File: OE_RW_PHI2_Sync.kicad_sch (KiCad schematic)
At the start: 2 parts, among them U5 74LS08, U9 74HC04

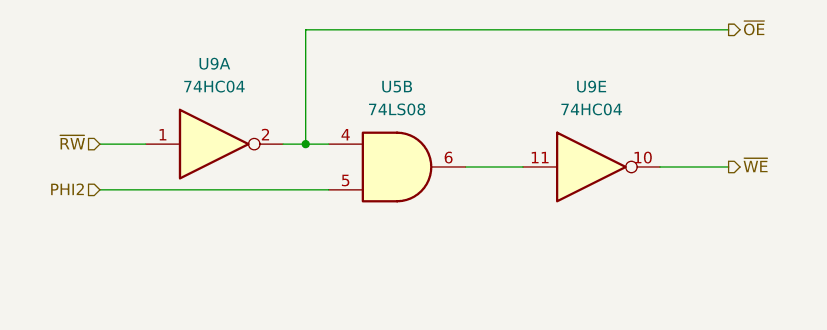
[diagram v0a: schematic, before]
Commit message: Rev 1 power section: run everything from the Pico's USB
- Pico 3V3 drives +3.3V, VBUS drives +5V for the header pins, and all
  GND pins plus AGND go to GND. VSYS is left free for a rev 2 power input.
  RUN, 3V3_EN, ADC_VREF and GP28 get no-connect flags.
- Decoupling: 100 nF per chip (C6-C13, each labelled with its chip) and
  22 uF bulk on +3.3V (C14).
- U5's only AND gate moves into U7's spare slot (U7B), and U5 is removed.
- U7 and U9 power units and spare gates are now on the sheet, with the
  spare gate inputs tied to GND so HC inputs don't float. U8's unused
  Y4-Y7 get no-connect flags.
- U7 74LS08 -> 74HC08, and U4 HM62256BLP -> AS6C62256-55PCN, because the
  LS08 and the HM62256 are 5 V-only parts.

Co-Authored-By: Claude Opus 5.5 <noreply@anthropic.com>
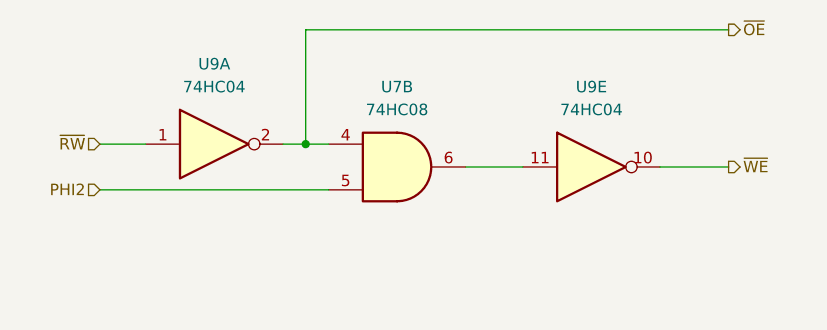
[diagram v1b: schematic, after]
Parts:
- U7: renamed from U5; value 74LS08 -> 74HC08
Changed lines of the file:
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@@
 		(dnp no)
 		(fields_autoplaced yes)
-		(property "Reference" "U5"
+		(property "Reference" "U7"
 			(at 140.9617 82.55 0)
 			(effects
@@
 			)
 		)
-		(property "Value" "74LS08"
+		(property "Value" "74HC08"
 			(at 140.9617 85.09 0)
 			(effects
@@
 			(project "Clementina-6502-Pico"
 				(path "/ddb0bb09-4973-4322-81e7-cdd57ff08282/6573b204-c090-453b-93ea-80574efd277d"
-					(reference "U5")
+					(reference "U7")
 					(unit 2)
 				)

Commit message: All through-hole parts: footprints, microSD breakout socket, round-pin jack
- Every part now has a through-hole footprint: DIP sockets for the chips,
  the Pico on 1x20 female headers (RaspberryPi_Pico_Common_THT), axial
  resistors and diodes, disc and radial capacitors, a 6 mm tactile switch.
- J5 is now a 1x9 female header for the Adafruit 4682 microSD breakout
  (3V, GND, CLK, SO, SI, CS, DAT1, DAT2, DET). The breakout has its own
  pull-ups and bypass caps, so RN1, C15 and C16 are gone. DAT1, DAT2 and
  DET are no-connects.
- J4 uses the CUI SJ1-3533NG footprint with round holes; the SJ1-3525N
  footprint needs 0.4 mm plated slots, below most hobby fabs' minimum.
- C3 and C5 (47 uF audio DC blocks) are drawn as polarized capacitors,
  + on the divider side.

Netlist unchanged apart from J5/RN1/C15/C16; ERC clean.

Co-Authored-By: Claude Opus 5.5 <noreply@anthropic.com>
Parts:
- U7, U9: footprint (none) -> Package_DIP:DIP-14_W7.62mm_Socket
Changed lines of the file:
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@@
 			)
 		)
-		(property "Footprint" ""
+		(property "Footprint" "Package_DIP:DIP-14_W7.62mm_Socket"
 			(at 162.56 91.44 0)
 			(effects
@@
 			)
 		)
-		(property "Footprint" ""
+		(property "Footprint" "Package_DIP:DIP-14_W7.62mm_Socket"
 			(at 140.97 91.44 0)
 			(effects
@@
 			)
 		)
-		(property "Footprint" ""
+		(property "Footprint" "Package_DIP:DIP-14_W7.62mm_Socket"
 			(at 120.65 88.9 0)
 			(effects

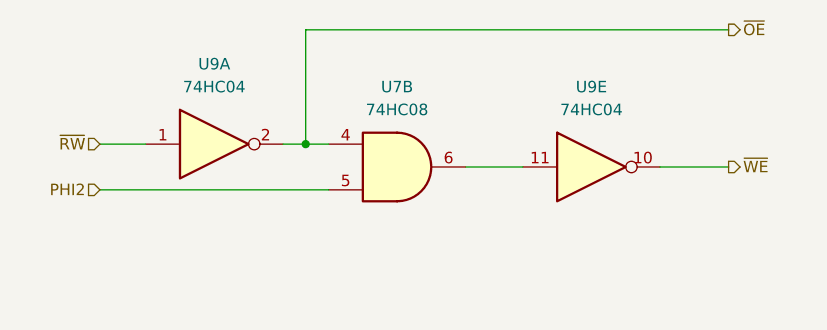
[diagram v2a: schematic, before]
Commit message: Glue logic: /WE from one NAND gate, flat I/O decode, 74AC parts
The write strobe went PHI2 -> 74HC08 -> 74HC04 -> /WE: about 26 ns typical
and up to ~65 ns at 3.3 V before /WE rose, against the W65C02S's 10 ns
address/data hold. With U4's /CE tied to A15, a store followed by an
access to another RAM address could also write that address.

- U9 is now a 74AC00 (quad NAND): ~OE = NAND(RWB, RWB),
  ~WE = NAND(PHI2, ~OE), MIASEL = NAND(~Y3, ~Y3), ~A15 = NAND(A15, A15).
  PHI2 reaches /WE through one gate (~5 ns typ, ~10 ns max as 74AC00),
  the same structure as the Picocomputer RP6502.
- U6 is enabled straight from the address (~E0 = A13, ~E1 = ~A15,
  E2 = A14) instead of through U8's ~Y2, removing one decoder level from
  the VIA/IOCS chip selects. U8 ~Y2 is now a no-connect.
- U7B becomes a spare (inputs to GND); U9's old spare inverters go.
- Values: U6/U8 74AC138, U7 74AC08, U9 74AC00 (all DIP).

The logic is unchanged (same truth tables). ERC clean.

Co-Authored-By: Claude Opus 5.5 <noreply@anthropic.com>
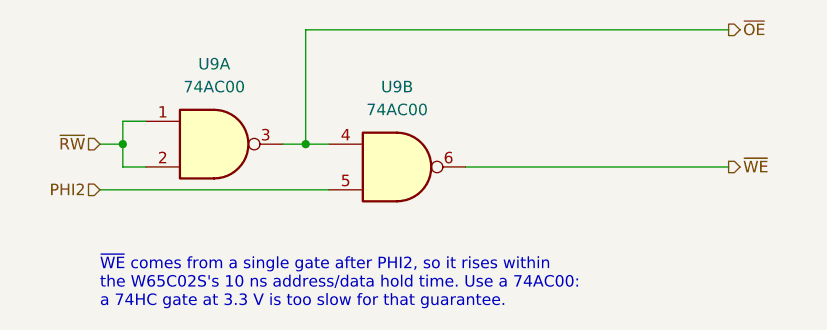
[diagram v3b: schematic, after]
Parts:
- removed U7: 74HC08, Package_DIP:DIP-14_W7.62mm_Socket, symbol 74xx:74LS08
- removed U9: 74HC04, Package_DIP:DIP-14_W7.62mm_Socket, symbol 74xx:74HC04
- added U9: 74AC00, Package_DIP:DIP-14_W7.62mm_Socket, symbol 74xx:74LS00
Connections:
- net PHI2: now also U9.5
- net ~{OE}: now also U9.3, U9.4
- net ~{RW}: now also U9.1, U9.2
- net ~{WE}: now also U9.6
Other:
- note added: "~{WE} comes from a single gate after PHI2, so it rises within the W65C02S's 10 ns address/data hold time. Use a 74AC00: a 74HC gate at 3.3 V is too slow for that guarantee."
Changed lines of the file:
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@@
-	(wire
-		(pts
-			(xy 170.18 91.44) (xy 177.8 91.44)
-		)
-		(stroke
-			(width 0)
-			(type default)
-		)
-	)
-	(wire
-		(pts
-			(xy 148.59 91.44) (xy 154.94 91.44)
-		)
-		(stroke
-			(width 0)
-			(type default)
-		)
-	)
-	(wire
-		(pts
-			(xy 107.95 88.9) (xy 113.03 88.9)
-		)
-		(stroke
-			(width 0)
-			(type default)
-		)
-	)
 	(wire
 		(pts
@@
 	)
 	(symbol
-		(lib_id "74xx:74HC04")
-		(at 162.56 91.44 0)
-		(unit 5)
+		(lib_id "74xx:74LS00")
+		(at 120.65 88.9 0)
+		(unit 1)
 		(exclude_from_sim no)
 		(in_bom yes)
 		(on_board yes)
 		(dnp no)
-		(fields_autoplaced yes)
 		(property "Reference" "U9"
-			(at 162.56 82.55 0)
-			(effects
-				(font
-					(size 1.27 1.27)
-				)
-			)
-		)
-		(property "Value" "74HC04"
-			(at 162.56 85.09 0)
+			(at 120.65 80.01 0)
+			(effects
+				(font
+					(size 1.27 1.27)
+				)
+			)
+		)
+		(property "Value" "74AC00"
+			(at 120.65 82.55 0)
 			(effects
 				(font
@@
 		)
 		(property "Footprint" "Package_DIP:DIP-14_W7.62mm_Socket"
-			(at 162.56 91.44 0)
-			(effects
-				(font
-					(size 1.27 1.27)
-				)
-				(hide yes)
-			)
-		)
-		(property "Datasheet" "https://assets.nexperia.com/documents/data-sheet/74HC_HCT04.pdf"
-			(at 162.56 91.44 0)
-			(effects
-				(font
-					(size 1.27 1.27)
-				)
-				(hide yes)
-			)
-		)
-		(property "Description" "Hex Inverter"
-			(at 162.56 91.44 0)
-			(effects
-				(font
-					(size 1.27 1.27)
-				)
-				(hide yes)
-			)
+			(at 120.65 88.9 0)
+			(effects
+				(font
+					(size 1.27 1.27)
+				)
+				(hide yes)
+			)
+		)
+		(property "Datasheet" "http://www.ti.com/lit/gpn/sn74ls00"
+			(at 120.65 88.9 0)
+			(effects
+				(font
+					(size 1.27 1.27)
+				)
+				(hide yes)
+			)
+		)
+		(property "Description" "quad 2-input NAND gate"
+			(at 120.65 88.9 0)
+			(effects
+				(font
+					(size 1.27 1.27)
+				)
+				(hide yes)
+			)
+		)
+		(pin "1"
+		)
+		(pin "2"
+		)
+		(pin "3"
+		)
+		(pin "4"
+		)
+		(pin "5"
+		)
+		(pin "6"
+		)
+		(pin "9"
+		)
+		(pin "10"
+		)
+		(pin "8"
+		)
+		(pin "12"
+		)
+		(pin "13"
+		)
+		(pin "11"
+		)
+		(pin "14"
 		)
 		(pin "7"
-		)
-		(pin "14"
-		)
-		(pin "12"
-		)
-		(pin "13"
-		)
-		(pin "10"
-		)
-		(pin "11"
-		)
-		(pin "8"
-		)
-		(pin "9"
-		)
-		(pin "6"
-		)
-		(pin "5"
-		)
-		(pin "4"
-		)
-		(pin "3"
-		)
-		(pin "2"
-		)
-		(pin "1"
 		)
 		(instances
@@
 				(path "/ddb0bb09-4973-4322-81e7-cdd57ff08282/6573b204-c090-453b-93ea-80574efd277d"
 					(reference "U9")
-					(unit 5)
-				)
-			)
-		)
+					(unit 1)
+				)
+			)
+		)
+	)
+	(wire
+		(pts
+			(xy 107.95 88.9) (xy 110.49 88.9)
+		)
+		(stroke
+			(width 0)
+			(type default)
+		)
+	)
+	(wire
+		(pts
+			(xy 110.49 86.36) (xy 110.49 88.9)
+		)
+		(stroke
+			(width 0)
+			(type default)
+		)
+	)
+	(wire
+		(pts
+			(xy 110.49 88.9) (xy 110.49 91.44)
+		)
+		(stroke
+			(width 0)
+			(type default)
+		)
+	)
+	(wire
+		(pts
+			(xy 110.49 86.36) (xy 113.03 86.36)
+		)
+		(stroke
+			(width 0)
+			(type default)
+		)
+	)
+	(wire
+		(pts
+			(xy 110.49 91.44) (xy 113.03 91.44)
+		)
+		(stroke
+			(width 0)
+			(type default)
+		)
+	)
+	(junction
+		(at 110.49 88.9)
+		(diameter 0)
+		(color 0 0 0 0)
 	)
 	(symbol
-		(lib_id "74xx:74LS08")
+		(lib_id "74xx:74LS00")
 		(at 140.97 91.44 0)
 		(unit 2)
@@
 		(on_board yes)
 		(dnp no)
-		(fields_autoplaced yes)
-		(property "Reference" "U7"
-			(at 140.9617 82.55 0)
-			(effects
-				(font
-					(size 1.27 1.27)
-				)
-			)
-		)
-		(property "Value" "74HC08"
-			(at 140.9617 85.09 0)
+		(property "Reference" "U9"
+			(at 140.97 82.55 0)
+			(effects
+				(font
+					(size 1.27 1.27)
+				)
+			)
+		)
+		(property "Value" "74AC00"
+			(at 140.97 85.09 0)
 			(effects
 				(font
@@
 			)
 		)
-		(property "Datasheet" "http://www.ti.com/lit/gpn/sn74LS08"
+		(property "Datasheet" "http://www.ti.com/lit/gpn/sn74ls00"
 			(at 140.97 91.44 0)
 			(effects
@@
 			)
 		)
-		(property "Description" "Quad And2"
+		(property "Description" "quad 2-input NAND gate"
 			(at 140.97 91.44 0)
 			(effects
@@
 			(project "Clementina-6502-Pico"
 				(path "/ddb0bb09-4973-4322-81e7-cdd57ff08282/6573b204-c090-453b-93ea-80574efd277d"
-					(reference "U7")
+					(reference "U9")
 					(unit 2)
 				)
@@
 		)
 	)
-	(symbol
-		(lib_id "74xx:74HC04")
-		(at 120.65 88.9 0)
-		(unit 1)
+	(wire
+		(pts
+			(xy 148.59 91.44) (xy 177.8 91.44)
+		)
+		(stroke
+			(width 0)
+			(type default)
+		)
+	)
+	(text "~{WE} comes from a single gate after PHI2, so it rises within\nthe W65C02S's 10 ns address/data hold time. Use a 74AC00:\na 74HC gate at 3.3 V is too slow for that guarantee."
 		(exclude_from_sim no)
-		(in_bom yes)
-		(on_board yes)
-		(dnp no)
-		(fields_autoplaced yes)
-		(property "Reference" "U9"
-			(at 120.65 80.01 0)
-			(effects
-				(font
-					(size 1.27 1.27)
-				)
-			)
-		)
-		(property "Value" "74HC04"
-			(at 120.65 82.55 0)
-			(effects
-				(font
-					(size 1.27 1.27)
-				)
-			)
-		)
-		(property "Footprint" "Package_DIP:DIP-14_W7.62mm_Socket"
-			(at 120.65 88.9 0)
-			(effects
-				(font
-					(size 1.27 1.27)
-				)
-				(hide yes)
-			)
-		)
-		(property "Datasheet" "https://assets.nexperia.com/documents/data-sheet/74HC_HCT04.pdf"
-			(at 120.65 88.9 0)
-			(effects
-				(font
-					(size 1.27 1.27)
-				)
-				(hide yes)
-			)
-		)
-		(property "Description" "Hex Inverter"
-			(at 120.65 88.9 0)
-			(effects
-				(font
-					(size 1.27 1.27)
-				)
-				(hide yes)
-			)
-		)
-		(pin "7"
-		)
-		(pin "14"
-		)
-		(pin "12"
-		)
-		(pin "13"
-		)
-		(pin "10"
-		)
-		(pin "11"
-		)
-		(pin "8"
-		)
-		(pin "9"
-		)
-		(pin "6"
-		)
-		(pin "5"
-		)
-		(pin "4"
-		)
-		(pin "3"
-		)
-		(pin "2"
-		)
-		(pin "1"
-		)
-		(instances
-			(project ""
-				(path "/ddb0bb09-4973-4322-81e7-cdd57ff08282/6573b204-c090-453b-93ea-80574efd277d"
-					(reference "U9")
-					(unit 1)
-				)
-			)
-		)
-	)
+		(at 107.95 101.6 0)
+		(effects
+			(font
+				(size 1.27 1.27)
+			)
+			(justify left top)
+		)
+	)

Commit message: Generic bill of materials for a solder-free build
Every part gets two hidden schematic fields:

- Factory: what is soldered at that designator, in generic terms (resistor
  value/size/pitch, capacitor type and lead spacing, DIP socket size for each
  chip, two 1x20 female headers for the Pico, box headers, jack, switch).
- Plug-in: what goes in afterwards (the chips, a Pico 2 WH with its pins
  pre-soldered, the Adafruit 4682).

bom/factory-bom.csv is generated from the Factory field with kicad-cli, so
the parts can be sourced by hand for the protoboard or given to an assembly
service. The README lists the plug-in parts and the regenerate command, and
notes that the 4682 ships with its header loose. Nets, ERC, DRC and parity
unchanged.

Co-Authored-By: Claude Opus 5.5 <noreply@anthropic.com>
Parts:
- U9: Factory (none) -> DIP-14 socket, 7.62 mm (0.3 in) rows; Plug-in (none) -> 74AC00 quad NAND, DIP-14
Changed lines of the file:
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@@
+			)
+		)
+		(property "Factory" "DIP-14 socket, 7.62 mm (0.3 in) rows"
+			(at 120.65 88.9 0)
+			(effects
+				(font
+					(size 1.27 1.27)
+				)
+				(hide yes)
+			)
+		)
+		(property "Plug-in" "74AC00 quad NAND, DIP-14"
+			(at 120.65 88.9 0)
+			(effects
+				(font
+					(size 1.27 1.27)
+				)
+				(hide yes)
 			)
 		)
@@
 			(at 140.97 91.44 0)
 			(effects
+				(font
+					(size 1.27 1.27)
+				)
+				(hide yes)
+			)
+		)
+		(property "Factory" "DIP-14 socket, 7.62 mm (0.3 in) rows"
+			(at 140.97 91.44 0)
+			(effects
+				(font
+					(size 1.27 1.27)
+				)
+				(hide yes)
+			)
+		)
+		(property "Plug-in" "74AC00 quad NAND, DIP-14"
+			(at 140.97 91.44 0)
+			(effects
